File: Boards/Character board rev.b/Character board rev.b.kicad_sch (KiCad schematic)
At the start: 64 parts, among them J1 card edge, J2 character connector, Q1 2N6125, U1 2.2K, U1 6821, U13 7406, U14 74LS42, U15 LM741, U16 AH5012, U2 2.2K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

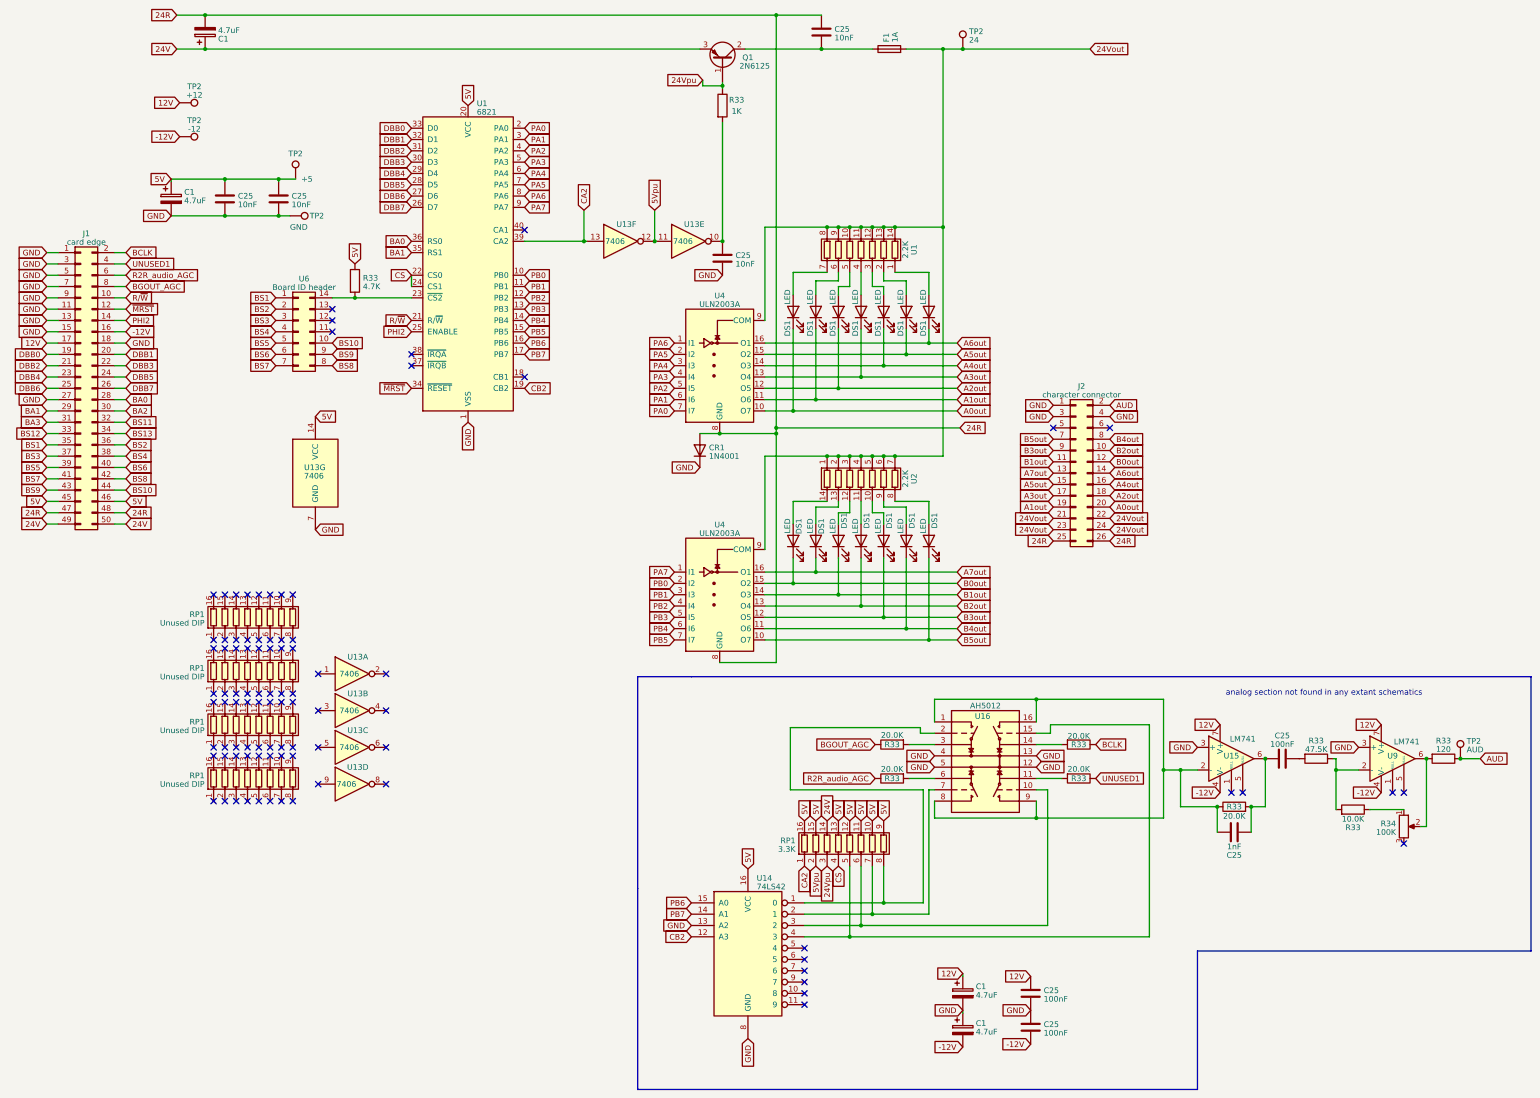
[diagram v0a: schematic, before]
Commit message: revised all net names to reflect new information about 4 channel audio system
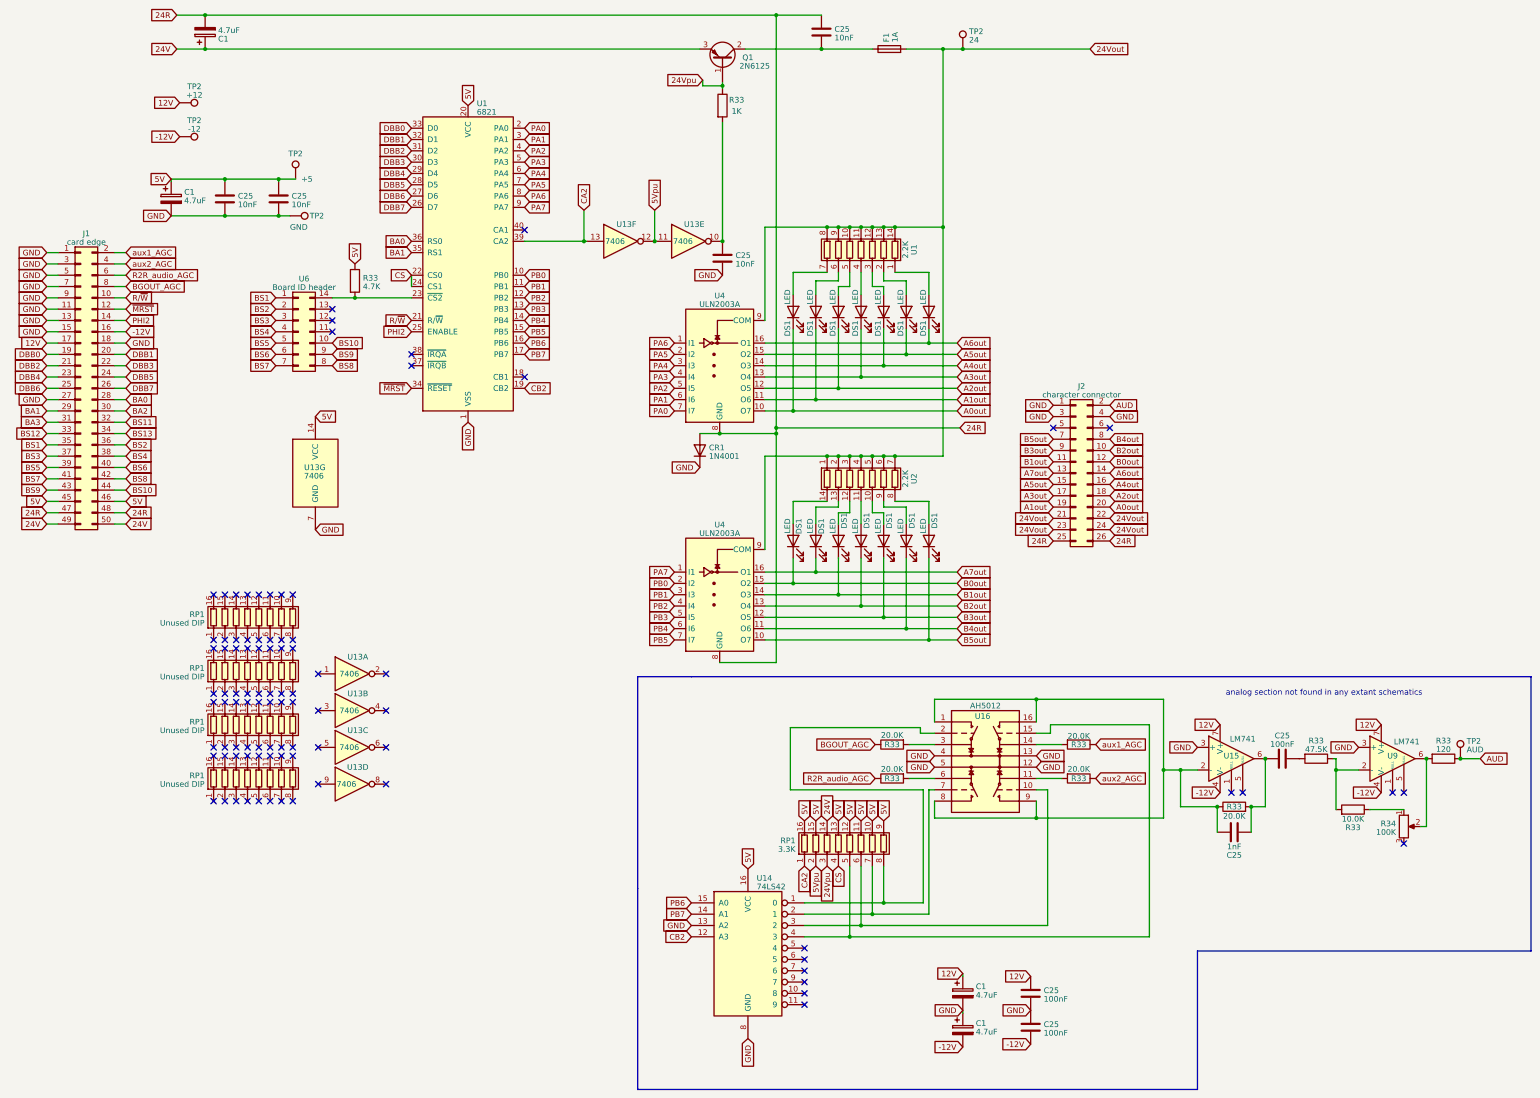
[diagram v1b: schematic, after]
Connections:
- net BCLK renamed aux1_AGC
- net UNUSED1 renamed aux2_AGC
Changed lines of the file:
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@@
     (effects (font (size 1.27 1.27)) (justify left bottom))
   )
-  (global_label "BCLK" (shape input) (at 48.895 72.39 0) (fields_autoplaced)
-    (effects (font (size 1.27 1.27)) (justify left))
-    (property "Intersheetrefs" "${INTERSHEET_REFS}" (at 56.6389 72.39 0)
+  (global_label "aux1_AGC" (shape input) (at 48.895 72.39 0) (fields_autoplaced)
+    (effects (font (size 1.27 1.27)) (justify left))
+    (property "Intersheetrefs" "${INTERSHEET_REFS}" (at 60.9326 72.39 0)
       (effects (font (size 1.27 1.27)) (justify left) hide)
     )
@@
     )
   )
-  (global_label "UNUSED1" (shape input) (at 48.895 74.93 0) (fields_autoplaced)
-    (effects (font (size 1.27 1.27)) (justify left))
-    (property "Intersheetrefs" "${INTERSHEET_REFS}" (at 60.6303 74.93 0)
+  (global_label "aux2_AGC" (shape input) (at 48.895 74.93 0) (fields_autoplaced)
+    (effects (font (size 1.27 1.27)) (justify left))
+    (property "Intersheetrefs" "${INTERSHEET_REFS}" (at 60.9326 74.93 0)
       (effects (font (size 1.27 1.27)) (justify left) hide)
     )
@@
     )
   )
-  (global_label "UNUSED1" (shape input) (at 266.7 190.5 0) (fields_autoplaced)
-    (effects (font (size 1.27 1.27)) (justify left))
-    (property "Intersheetrefs" "${INTERSHEET_REFS}" (at 278.4353 190.5 0)
+  (global_label "aux2_AGC" (shape input) (at 266.7 190.5 0) (fields_autoplaced)
+    (effects (font (size 1.27 1.27)) (justify left))
+    (property "Intersheetrefs" "${INTERSHEET_REFS}" (at 278.7376 190.5 0)
       (effects (font (size 1.27 1.27)) (justify left) hide)
     )
@@
     )
   )
-  (global_label "BCLK" (shape input) (at 266.7 182.88 0) (fields_autoplaced)
-    (effects (font (size 1.27 1.27)) (justify left))
-    (property "Intersheetrefs" "${INTERSHEET_REFS}" (at 274.4439 182.88 0)
-      (effects (font (size 1.27 1.27)) (justify left) hide)
-    )
+  (global_label "aux1_AGC" (shape input) (at 266.7 182.88 0) (fields_autoplaced)
+    (effects (font (size 1.27 1.27)) (justify left))
+    (property "Intersheetrefs" "${INTERSHEET_REFS}" (at 278.7376 182.88 0)
+      (effects (font (size 1.27 1.27)) (justify left) hide)
+    )
